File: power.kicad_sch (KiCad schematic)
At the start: 57 parts, among them J12 Barrel_Jack_Switch, J13 Conn_02x05_Odd_Even, J14 Screw_Terminal_01x12, U14 LP38692MP-5.0, U15 LP38693MP-3.3, U16 LM2937xMP, U17 MAX6070BAUT21+T, U18 LP38693MP-1.8, U19 MC79M15_TO252, U20 LP38693MP-2.5

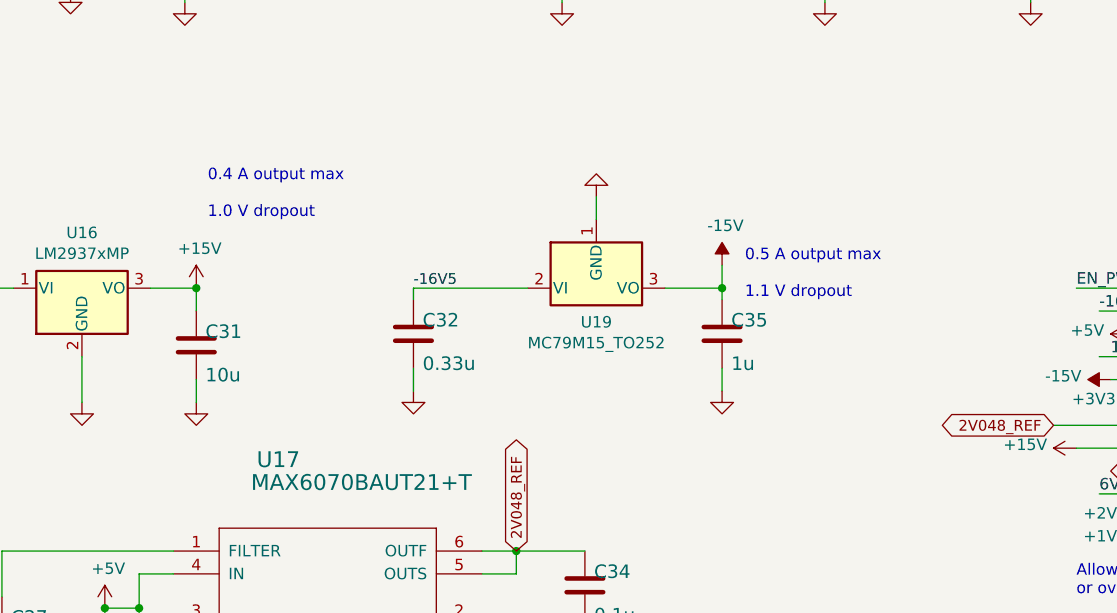
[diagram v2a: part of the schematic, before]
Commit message: deleted fab files and doc files not relevant to this branch
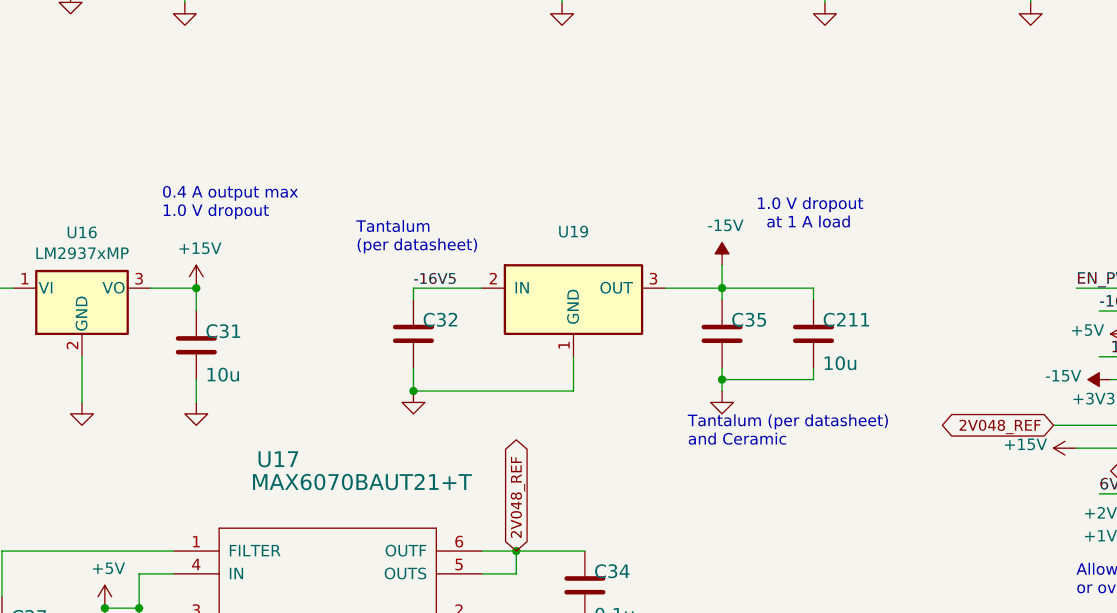
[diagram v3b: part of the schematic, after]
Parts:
- removed U19: MC79M15_TO252, Package_TO_SOT_SMD:TO-252-2, symbol Regulator_Linear:MC79M15_TO252
- added C211: 10u, Capacitor_SMD:C_0805_2012Metric, symbol Device:C
- added U19: (no value), symbol Regulator_Linear:LM2990SX-15
- C32: value 0.33u -> (none); footprint Capacitor_SMD:C_0603_1608Metric -> (none); Manf# CC0603KRX5R8BB334 -> TAJA105K025RNJ; Manufacturer_Name Yageo -> (none); Tolerance 10% -> (none)
- C35: value 1u -> (none); footprint Capacitor_SMD:C_0603_1608Metric -> (none); Manf# CL10A105KA8NFNC -> TAJA105K025RNJ
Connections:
- net -15V: now also C211.1, U19.3 (OUT)
- net -16V5: now also U19.2 (IN)
- net GND: now also C211.2, U19.1 (GND)
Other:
- note added: "1.0 V dropout at 1 A load"
- note added: "Tantalum (per datasheet)"
- note added: "Tantalum (per datasheet) and Ceramic"
- note removed: "0.5 A output max 1.1 V dropout"
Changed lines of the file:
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@@
   (junction (at 213.36 72.39) (diameter 0) (color 0 0 0 0)
   )
+  (junction (at 242.57 115.57) (diameter 0) (color 0 0 0 0)
+  )
   (junction (at 257.81 58.42) (diameter 0) (color 0 0 0 0)
   )
@@
   (junction (at 223.52 142.24) (diameter 0) (color 0 0 0 0)
   )
+  (junction (at 208.28 116.84) (diameter 0) (color 0 0 0 0)
+  )
   (no_connect (at 27.94 59.69))
   (wire (pts (xy 55.88 21.59) (xy 55.88 27.94))
@@
     (stroke (width 0) (type default) (color 0 0 0 0))
   )
+  (wire (pts (xy 242.57 115.57) (xy 252.73 115.57))
+    (stroke (width 0) (type default) (color 0 0 0 0))
+  )
   (wire (pts (xy 284.48 107.95) (xy 292.1 107.95))
     (stroke (width 0) (type default) (color 0 0 0 0))
@@
     (stroke (width 0) (type default) (color 0 0 0 0))
   )
+  (wire (pts (xy 242.57 105.41) (xy 252.73 105.41))
+    (stroke (width 0) (type default) (color 0 0 0 0))
+  )
   (wire (pts (xy 82.55 72.39) (xy 63.5 72.39))
     (stroke (width 0) (type default) (color 0 0 0 0))
@@
     (stroke (width 0) (type default) (color 0 0 0 0))
   )
-  (wire (pts (xy 242.57 114.3) (xy 242.57 116.84))
+  (wire (pts (xy 242.57 114.3) (xy 242.57 115.57))
     (stroke (width 0) (type default) (color 0 0 0 0))
   )
@@
     (stroke (width 0) (type default) (color 0 0 0 0))
   )
-  (wire (pts (xy 208.28 105.41) (xy 220.98 105.41))
-    (stroke (width 0) (type default) (color 0 0 0 0))
-  )
   (wire (pts (xy 182.88 69.85) (xy 182.88 72.39))
     (stroke (width 0) (type default) (color 0 0 0 0))
@@
     (stroke (width 0) (type default) (color 0 0 0 0))
   )
+  (wire (pts (xy 226.06 113.03) (xy 226.06 116.84))
+    (stroke (width 0) (type default) (color 0 0 0 0))
+  )
   (wire (pts (xy 116.84 114.3) (xy 116.84 118.11))
     (stroke (width 0) (type default) (color 0 0 0 0))
@@
     (stroke (width 0) (type default) (color 0 0 0 0))
   )
+  (wire (pts (xy 252.73 105.41) (xy 252.73 106.68))
+    (stroke (width 0) (type default) (color 0 0 0 0))
+  )
   (wire (pts (xy 292.1 72.39) (xy 292.1 73.66))
     (stroke (width 0) (type default) (color 0 0 0 0))
@@
     (stroke (width 0) (type default) (color 0 0 0 0))
   )
+  (wire (pts (xy 242.57 115.57) (xy 242.57 116.84))
+    (stroke (width 0) (type default) (color 0 0 0 0))
+  )
   (wire (pts (xy 60.96 123.19) (xy 59.69 123.19))
     (stroke (width 0) (type default) (color 0 0 0 0))
@@
     (stroke (width 0) (type default) (color 0 0 0 0))
   )
+  (wire (pts (xy 208.28 105.41) (xy 215.9 105.41))
+    (stroke (width 0) (type default) (color 0 0 0 0))
+  )
   (wire (pts (xy 91.44 123.19) (xy 95.25 123.19))
     (stroke (width 0) (type default) (color 0 0 0 0))
@@
     (stroke (width 0) (type default) (color 0 0 0 0))
   )
+  (wire (pts (xy 252.73 114.3) (xy 252.73 115.57))
+    (stroke (width 0) (type default) (color 0 0 0 0))
+  )
   (wire (pts (xy 116.84 104.14) (xy 110.49 104.14))
     (stroke (width 0) (type default) (color 0 0 0 0))
@@
     (stroke (width 0) (type default) (color 0 0 0 0))
   )
+  (wire (pts (xy 208.28 116.84) (xy 226.06 116.84))
+    (stroke (width 0) (type default) (color 0 0 0 0))
+  )
   (wire (pts (xy 163.83 58.42) (xy 170.18 58.42))
     (stroke (width 0) (type default) (color 0 0 0 0))
@@
     (stroke (width 0) (type default) (color 0 0 0 0))
   )
-  (wire (pts (xy 228.6 95.25) (xy 228.6 97.79))
-    (stroke (width 0) (type default) (color 0 0 0 0))
-  )
   (wire (pts (xy 45.72 104.14) (xy 50.8 104.14))
     (stroke (width 0) (type default) (color 0 0 0 0))
@@
     (effects (font (size 1.4986 1.4986)) (justify left bottom))
   )
+  (text "Tantalum \n(per datasheet)" (at 201.93 101.6 0)
+    (effects (font (size 1.27 1.27)) (justify left bottom))
+  )
   (text "1 A output" (at 88.9 53.34 0)
     (effects (font (size 1.4986 1.4986)) (justify left bottom))
@@
     (effects (font (size 1.27 1.27)) (justify left bottom))
   )
-  (text "0.4 A output max\n\n1.0 V dropout" (at 185.42 97.79 0)
+  (text "0.4 A output max\n1.0 V dropout" (at 180.34 97.79 0)
     (effects (font (size 1.27 1.27)) (justify left bottom))
   )
@@
     (effects (font (size 0.9906 0.9906)) (justify left bottom))
   )
-  (text "0.5 A output max\n\n1.1 V dropout" (at 245.11 106.68 0)
+  (text "1.0 V dropout \n  at 1 A load\n" (at 246.38 99.06 0)
     (effects (font (size 1.27 1.27)) (justify left bottom))
   )
@@
     (effects (font (size 1.27 1.27)) (justify left bottom))
   )
+  (text "Tantalum (per datasheet)\nand Ceramic" (at 238.76 123.19 0)
+    (effects (font (size 1.27 1.27)) (justify left bottom))
+  )
   (text "Vin up to 10 V\nEN min is 3V with 6 V Vin" (at 179.07 50.8 0)
     (effects (font (size 1.4986 1.4986)) (justify left bottom))
@@
       (effects (font (size 1.4986 1.4986)) (justify left bottom))
     )
-    (property "Value" "1u" (id 1) (at 243.586 114.681 0)
+    (property "Value" "" (id 1) (at 243.586 114.681 0)
       (effects (font (size 1.4986 1.4986)) (justify left bottom))
     )
-    (property "Footprint" "Capacitor_SMD:C_0603_1608Metric" (id 2) (at 242.57 110.49 0)
+    (property "Footprint" "" (id 2) (at 242.57 110.49 0)
       (effects (font (size 1.27 1.27)) hide)
     )
@@
       (effects (font (size 1.27 1.27)) hide)
     )
-    (property "Manf#" "CL10A105KA8NFNC" (id 4) (at 243.586 107.315 0)
+    (property "Manf#" "TAJA105K025RNJ" (id 4) (at 243.586 107.315 0)
       (effects (font (size 1.27 1.27)) hide)
     )
@@
     (pin "1")
   )
-  (symbol (lib_id "Regulator_Linear:MC79M15_TO252") (at 228.6 105.41 0) (unit 1)
-    (in_bom yes) (on_board yes)
-    (property "Reference" "U19" (id 0) (at 228.6 109.1946 0))
-    (property "Value" "MC79M15_TO252" (id 1) (at 228.6 111.506 0))
-    (property "Footprint" "Package_TO_SOT_SMD:TO-252-2" (id 2) (at 228.6 110.49 0)
-      (effects (font (size 1.27 1.27) italic) hide)
-    )
-    (property "Datasheet" "http://www.onsemi.com/pub/Collateral/MC79M00-D.PDF" (id 3) (at 228.6 105.41 0)
-      (effects (font (size 1.27 1.27)) hide)
-    )
-    (property "Manf#" "MC79M15BDTRKG" (id 4) (at 228.6 106.6546 0)
-      (effects (font (size 1.27 1.27)) hide)
-    )
-    (pin "1")
-    (pin "2")
-    (pin "3")
-  )
-  (symbol (lib_id "power:GND") (at 228.6 95.25 180) (unit 1)
-    (in_bom yes) (on_board yes)
-    (property "Reference" "#GND052" (id 0) (at 228.6 95.25 0)
-      (effects (font (size 1.27 1.27)) hide)
-    )
-    (property "Value" "GND" (id 1) (at 231.14 92.71 0)
-      (effects (font (size 1.4986 1.4986)) (justify left bottom) hide)
-    )
-    (property "Footprint" "" (id 2) (at 228.6 95.25 0)
-      (effects (font (size 1.27 1.27)) hide)
-    )
-    (property "Datasheet" "" (id 3) (at 228.6 95.25 0)
-      (effects (font (size 1.27 1.27)) hide)
-    )
-    (pin "1")
-  )
   (symbol (lib_id "Regulator_Linear:LP38693MP-5.0") (at 82.55 60.96 0) (unit 1)
     (in_bom yes) (on_board yes)
@@
       (effects (font (size 1.4986 1.4986)) (justify left bottom))
     )
-    (property "Value" "0.33u" (id 1) (at 209.296 114.681 0)
+    (property "Value" "" (id 1) (at 209.296 114.681 0)
       (effects (font (size 1.4986 1.4986)) (justify left bottom))
     )
-    (property "Footprint" "Capacitor_SMD:C_0603_1608Metric" (id 2) (at 208.28 110.49 0)
+    (property "Footprint" "" (id 2) (at 208.28 110.49 0)
       (effects (font (size 1.27 1.27)) hide)
     )
@@
       (effects (font (size 1.27 1.27)) hide)
     )
-    (property "Manf#" "CC0603KRX5R8BB334" (id 4) (at 209.296 107.315 0)
+    (property "Manf#" "TAJA105K025RNJ" (id 4) (at 209.296 107.315 0)
       (effects (font (size 1.27 1.27)) hide)
     )
-    (property "Manufacturer_Name" "Yageo" (id 5) (at 209.296 107.315 0)
+    (property "Manufacturer_Name" "" (id 5) (at 209.296 107.315 0)
       (effects (font (size 1.27 1.27)) hide)
     )
-    (property "Tolerance" "10%" (id 6) (at 209.296 107.315 0)
+    (property "Tolerance" "" (id 6) (at 209.296 107.315 0)
       (effects (font (size 1.27 1.27)) hide)
     )
@@
     (pin "1")
   )
+  (symbol (lib_id "Device:C") (at 252.73 110.49 0) (unit 1)
+    (in_bom yes) (on_board yes)
+    (property "Reference" "C211" (id 0) (at 253.746 109.855 0)
+      (effects (font (size 1.4986 1.4986)) (justify left bottom))
+    )
+    (property "Value" "10u" (id 1) (at 253.746 114.681 0)
+      (effects (font (size 1.4986 1.4986)) (justify left bottom))
+    )
+    (property "Footprint" "Capacitor_SMD:C_0805_2012Metric" (id 2) (at 252.73 110.49 0)
+      (effects (font (size 1.27 1.27)) hide)
+    )
+    (property "Datasheet" "" (id 3) (at 252.73 110.49 0)
+      (effects (font (size 1.27 1.27)) hide)
+    )
+    (property "Manf#" "TMK212BBJ106MG-T" (id 4) (at 253.746 107.315 0)
+      (effects (font (size 1.27 1.27)) hide)
+    )
+    (property "Manufacturer_Name" "Taiyo Yuden" (id 5) (at 253.746 107.315 0)
+      (effects (font (size 1.27 1.27)) hide)
+    )
+    (property "Tolerance" "20%" (id 6) (at 253.746 107.315 0)
+      (effects (font (size 1.27 1.27)) hide)
+    )
+    (property "voltage" "25" (id 7) (at 253.746 107.315 0)
+      (effects (font (size 1.27 1.27)) hide)
+    )
+    (pin "1")
+    (pin "2")
+  )
+  (symbol (lib_id "Regulator_Linear:LM2990SX-15") (at 226.06 105.41 0) (unit 1)
+    (in_bom yes) (on_board yes) (fields_autoplaced)
+    (property "Reference" "U19" (id 0) (at 226.06 99.1702 0))
+    (property "Value" "" (id 1) (at 226.06 101.7071 0))
+    (property "Footprint" "" (id 2) (at 226.06 115.57 0)
+      (effects (font (size 1.27 1.27)) hide)
+    )
+    (property "Datasheet" "http://www.ti.com/lit/ds/symlink/lm2990.pdf" (id 3) (at 194.31 86.36 0)
+      (effects (font (size 1.27 1.27)) hide)
+    )
+    (pin "1")
+    (pin "2")
+    (pin "3")
+  )
 )
